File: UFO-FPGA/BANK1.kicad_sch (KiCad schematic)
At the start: 7 parts, among them U1 ICE40HX8K-BG121

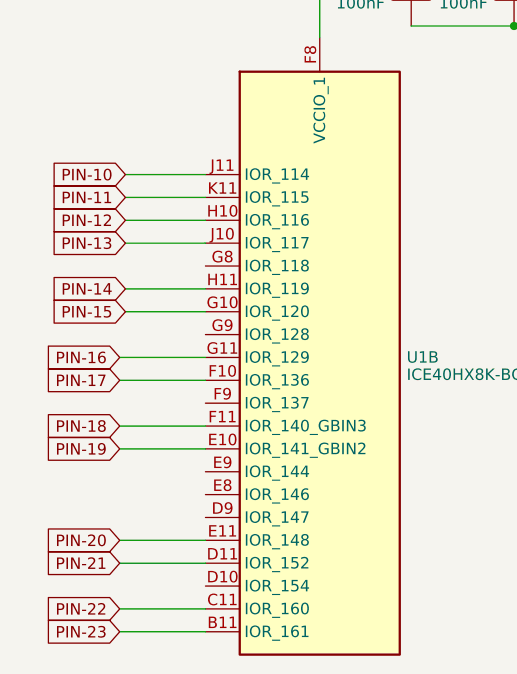
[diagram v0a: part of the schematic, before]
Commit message: Opamp gemaakt van de ADC
Enkel nog begrijpen wat VDC is. Aan docent vragen?
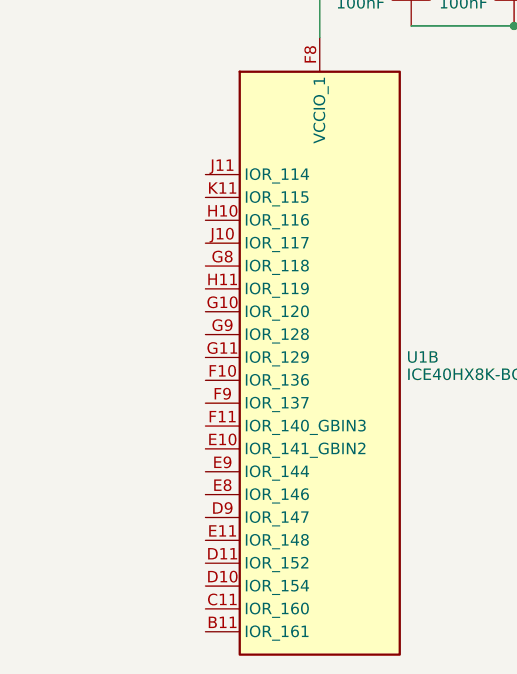
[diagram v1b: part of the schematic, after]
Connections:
- net PIN-10: no longer names the net of U1.J11 (IOR_114)
- net PIN-11: no longer names the net of U1.K11 (IOR_115)
- net PIN-12: no longer names the net of U1.H10 (IOR_116)
- net PIN-13: no longer names the net of U1.J10 (IOR_117)
- net PIN-14: no longer names the net of U1.H11 (IOR_119)
- net PIN-15: no longer names the net of U1.G10 (IOR_120)
- net PIN-16: no longer names the net of U1.G11 (IOR_129)
- net PIN-17: no longer names the net of U1.F10 (IOR_136)
- net PIN-18: no longer names the net of U1.F11 (IOR_140_GBIN3)
- net PIN-19: no longer names the net of U1.E10 (IOR_141_GBIN2)
- net PIN-20: no longer names the net of U1.E11 (IOR_148)
- net PIN-21: no longer names the net of U1.D11 (IOR_152)
- net PIN-22: no longer names the net of U1.C11 (IOR_160)
- net PIN-23: no longer names the net of U1.B11 (IOR_161)
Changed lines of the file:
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@@
   (junction (at 168.91 38.1) (diameter 0) (color 0 0 0 0)
   )
-  (wire (pts (xy 100.965 110.49) (xy 110.49 110.49))
-    (stroke (width 0) (type default))
-  )
   (wire (pts (xy 156.21 38.1) (xy 144.78 38.1))
-    (stroke (width 0) (type default))
-  )
-  (wire (pts (xy 100.965 90.17) (xy 110.49 90.17))
-    (stroke (width 0) (type default))
-  )
-  (wire (pts (xy 101.6 62.23) (xy 110.49 62.23))
-    (stroke (width 0) (type default))
-  )
-  (wire (pts (xy 101.6 64.77) (xy 110.49 64.77))
-    (stroke (width 0) (type default))
-  )
-  (wire (pts (xy 101.6 67.31) (xy 110.49 67.31))
-    (stroke (width 0) (type default))
-  )
-  (wire (pts (xy 101.6 74.93) (xy 110.49 74.93))
     (stroke (width 0) (type default))
   )
@@
     (stroke (width 0) (type default))
   )
-  (wire (pts (xy 100.965 113.03) (xy 110.49 113.03))
-    (stroke (width 0) (type default))
-  )
   (wire (pts (xy 156.21 45.72) (xy 144.78 45.72))
-    (stroke (width 0) (type default))
-  )
-  (wire (pts (xy 100.965 92.71) (xy 110.49 92.71))
     (stroke (width 0) (type default))
   )
@@
     (stroke (width 0) (type default))
   )
-  (wire (pts (xy 101.6 77.47) (xy 110.49 77.47))
-    (stroke (width 0) (type default))
-  )
   (wire (pts (xy 168.91 38.1) (xy 179.07 38.1))
     (stroke (width 0) (type default))
@@
     (stroke (width 0) (type default))
   )
-  (wire (pts (xy 100.965 85.09) (xy 110.49 85.09))
-    (stroke (width 0) (type default))
-  )
   (wire (pts (xy 168.91 38.1) (xy 167.64 38.1))
-    (stroke (width 0) (type default))
-  )
-  (wire (pts (xy 100.965 105.41) (xy 110.49 105.41))
-    (stroke (width 0) (type default))
-  )
-  (wire (pts (xy 101.6 69.85) (xy 110.49 69.85))
-    (stroke (width 0) (type default))
-  )
-  (wire (pts (xy 100.965 82.55) (xy 110.49 82.55))
     (stroke (width 0) (type default))
   )
@@
     (stroke (width 0) (type default))
   )
-  (wire (pts (xy 100.965 102.87) (xy 110.49 102.87))
-    (stroke (width 0) (type default))
-  )
   (label "VCCIO_1" (at 123.19 38.1 0) (fields_autoplaced)
     (effects (font (size 1.27 1.27)) (justify left bottom))
   )
-  (global_label "PIN-20" (shape input) (at 100.965 102.87 180) (fields_autoplaced)
-    (effects (font (size 1.27 1.27)) (justify right))
-    (property "Intersheetrefs" "${INTERSHEET_REFS}" (at 90.8625 102.87 0)
-      (effects (font (size 1.27 1.27)) (justify right) hide)
-    )
-  )
-  (global_label "PIN-15" (shape input) (at 101.6 77.47 180) (fields_autoplaced)
-    (effects (font (size 1.27 1.27)) (justify right))
-    (property "Intersheetrefs" "${INTERSHEET_REFS}" (at 91.4975 77.47 0)
-      (effects (font (size 1.27 1.27)) (justify right) hide)
-    )
-  )
-  (global_label "PIN-10" (shape input) (at 101.6 62.23 180) (fields_autoplaced)
-    (effects (font (size 1.27 1.27)) (justify right))
-    (property "Intersheetrefs" "${INTERSHEET_REFS}" (at 91.4975 62.23 0)
-      (effects (font (size 1.27 1.27)) (justify right) hide)
-    )
-  )
-  (global_label "PIN-22" (shape input) (at 100.965 110.49 180) (fields_autoplaced)
-    (effects (font (size 1.27 1.27)) (justify right))
-    (property "Intersheetrefs" "${INTERSHEET_REFS}" (at 90.8625 110.49 0)
-      (effects (font (size 1.27 1.27)) (justify right) hide)
-    )
-  )
-  (global_label "PIN-11" (shape input) (at 101.6 64.77 180) (fields_autoplaced)
-    (effects (font (size 1.27 1.27)) (justify right))
-    (property "Intersheetrefs" "${INTERSHEET_REFS}" (at 91.4975 64.77 0)
-      (effects (font (size 1.27 1.27)) (justify right) hide)
-    )
-  )
-  (global_label "PIN-13" (shape input) (at 101.6 69.85 180) (fields_autoplaced)
-    (effects (font (size 1.27 1.27)) (justify right))
-    (property "Intersheetrefs" "${INTERSHEET_REFS}" (at 91.4975 69.85 0)
-      (effects (font (size 1.27 1.27)) (justify right) hide)
-    )
-  )
-  (global_label "PIN-18" (shape input) (at 100.965 90.17 180) (fields_autoplaced)
-    (effects (font (size 1.27 1.27)) (justify right))
-    (property "Intersheetrefs" "${INTERSHEET_REFS}" (at 90.8625 90.17 0)
-      (effects (font (size 1.27 1.27)) (justify right) hide)
-    )
-  )
-  (global_label "PIN-19" (shape input) (at 100.965 92.71 180) (fields_autoplaced)
-    (effects (font (size 1.27 1.27)) (justify right))
-    (property "Intersheetrefs" "${INTERSHEET_REFS}" (at 90.8625 92.71 0)
-      (effects (font (size 1.27 1.27)) (justify right) hide)
-    )
-  )
-  (global_label "PIN-14" (shape input) (at 101.6 74.93 180) (fields_autoplaced)
-    (effects (font (size 1.27 1.27)) (justify right))
-    (property "Intersheetrefs" "${INTERSHEET_REFS}" (at 91.4975 74.93 0)
-      (effects (font (size 1.27 1.27)) (justify right) hide)
-    )
-  )
-  (global_label "PIN-12" (shape input) (at 101.6 67.31 180) (fields_autoplaced)
-    (effects (font (size 1.27 1.27)) (justify right))
-    (property "Intersheetrefs" "${INTERSHEET_REFS}" (at 91.4975 67.31 0)
-      (effects (font (size 1.27 1.27)) (justify right) hide)
-    )
-  )
-  (global_label "PIN-16" (shape input) (at 100.965 82.55 180) (fields_autoplaced)
-    (effects (font (size 1.27 1.27)) (justify right))
-    (property "Intersheetrefs" "${INTERSHEET_REFS}" (at 90.8625 82.55 0)
-      (effects (font (size 1.27 1.27)) (justify right) hide)
-    )
-  )
-  (global_label "PIN-17" (shape input) (at 100.965 85.09 180) (fields_autoplaced)
-    (effects (font (size 1.27 1.27)) (justify right))
-    (property "Intersheetrefs" "${INTERSHEET_REFS}" (at 90.8625 85.09 0)
-      (effects (font (size 1.27 1.27)) (justify right) hide)
-    )
-  )
-  (global_label "PIN-23" (shape input) (at 100.965 113.03 180) (fields_autoplaced)
-    (effects (font (size 1.27 1.27)) (justify right))
-    (property "Intersheetrefs" "${INTERSHEET_REFS}" (at 90.8625 113.03 0)
-      (effects (font (size 1.27 1.27)) (justify right) hide)
-    )
-  )
-  (global_label "PIN-21" (shape input) (at 100.965 105.41 180) (fields_autoplaced)
-    (effects (font (size 1.27 1.27)) (justify right))
-    (property "Intersheetrefs" "${INTERSHEET_REFS}" (at 90.8625 105.41 0)
-      (effects (font (size 1.27 1.27)) (justify right) hide)
-    )
-  )
   (symbol (lib_id "FPGA_Lattice:ICE40HX8K-BG121") (at 123.19 82.55 0) (unit 2)

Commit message: IO and power
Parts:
- removed C17 (x3): 100nF, symbol Device:C
- added C17 (x3): 100nF, symbol Device:C
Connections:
- net GND: now also C17.2, C17.2, C17.2
- net VCCIO_1: now also C17.1, C17.1, C17.1
- net PIN-23: now reaches U1.B11 (IOR_161)
- net PIN-22: now reaches U1.C11 (IOR_160)
- net PIN-21: now reaches U1.D11 (IOR_152)
- net PIN-19: now reaches U1.E10 (IOR_141_GBIN2)
- net PIN-20: now reaches U1.E11 (IOR_148)
- net PIN-17: now reaches U1.F10 (IOR_136)
- net PIN-18: now reaches U1.F11 (IOR_140_GBIN3)
- net PIN-15: now reaches U1.G10 (IOR_120)
- net PIN-16: now reaches U1.G11 (IOR_129)
- net PIN-12: now reaches U1.H10 (IOR_116)
- net PIN-14: now reaches U1.H11 (IOR_119)
- net PIN-13: now reaches U1.J10 (IOR_117)
- net PIN-10: now reaches U1.J11 (IOR_114)
- net PIN-11: now reaches U1.K11 (IOR_115)

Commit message: Revision
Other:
- company: (none) -> Universal-Field-Objects
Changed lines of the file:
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@@
   (paper "A4")
   (title_block
-    (date "2023-04-22")
-    (rev "V0.1")
+    (date "2023-04-25")
+    (rev "V0.5")
+    (company "Universal-Field-Objects")
   )
   (junction (at 182.88 55.88) (diameter 0) (color 0 0 0 0)

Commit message: footprints and PCB
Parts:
- R25: footprint (none) -> Resistor_SMD:R_0805_2012Metric_Pad1.20x1.40mm_HandSolder
- TP8: footprint (none) -> TestPoint:TestPoint_Keystone_5000-5004_Miniature
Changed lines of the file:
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@@
       (effects (font (size 1.27 1.27)) (justify left))
     )
-    (property "Footprint" "" (at 189.23 48.26 0)
+    (property "Footprint" "TestPoint:TestPoint_Keystone_5000-5004_Miniature" (at 189.23 48.26 0)
       (effects (font (size 1.27 1.27)) hide)
     )
@@
       (effects (font (size 1.27 1.27)))
     )
-    (property "Footprint" "" (at 198.12 46.482 90)
+    (property "Footprint" "Resistor_SMD:R_0805_2012Metric_Pad1.20x1.40mm_HandSolder" (at 198.12 46.482 90)
       (effects (font (size 1.27 1.27)) hide)
     )

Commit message: footprint
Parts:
- C17, C18: footprint (none) -> Capacitor_SMD:C_0805_2012Metric_Pad1.18x1.45mm_HandSolder
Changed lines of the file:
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@@
       (effects (font (size 1.27 1.27)) (justify left))
     )
-    (property "Footprint" "" (at 147.6248 55.88 0)
+    (property "Footprint" "Capacitor_SMD:C_0805_2012Metric_Pad1.18x1.45mm_HandSolder" (at 147.6248 55.88 0)
       (effects (font (size 1.27 1.27)) hide)
     )
@@
       (effects (font (size 1.27 1.27)) (justify left))
     )
-    (property "Footprint" "" (at 181.9148 55.88 0)
+    (property "Footprint" "Capacitor_SMD:C_0805_2012Metric_Pad1.18x1.45mm_HandSolder" (at 181.9148 55.88 0)
       (effects (font (size 1.27 1.27)) hide)
     )
@@
       (effects (font (size 1.27 1.27)) (justify left))
     )
-    (property "Footprint" "" (at 170.4848 55.88 0)
+    (property "Footprint" "Capacitor_SMD:C_0805_2012Metric_Pad1.18x1.45mm_HandSolder" (at 170.4848 55.88 0)
       (effects (font (size 1.27 1.27)) hide)
     )
@@
       (effects (font (size 1.27 1.27)) (justify left))
     )
-    (property "Footprint" "" (at 159.0548 55.88 0)
+    (property "Footprint" "Capacitor_SMD:C_0805_2012Metric_Pad1.18x1.45mm_HandSolder" (at 159.0548 55.88 0)
       (effects (font (size 1.27 1.27)) hide)
     )

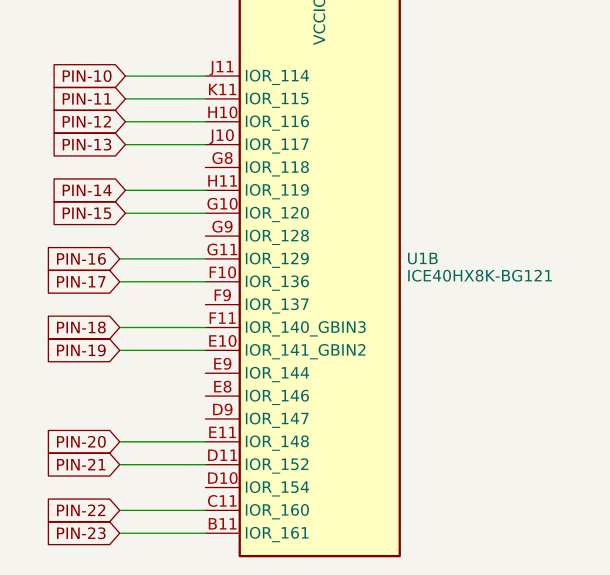
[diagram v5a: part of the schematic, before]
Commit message: PCB planes
Added:
added Power plane +1v2, +3v3 and +5v on layer 4
Ground plane on layer 2 and 5
Added signal layer 1,3 and 6
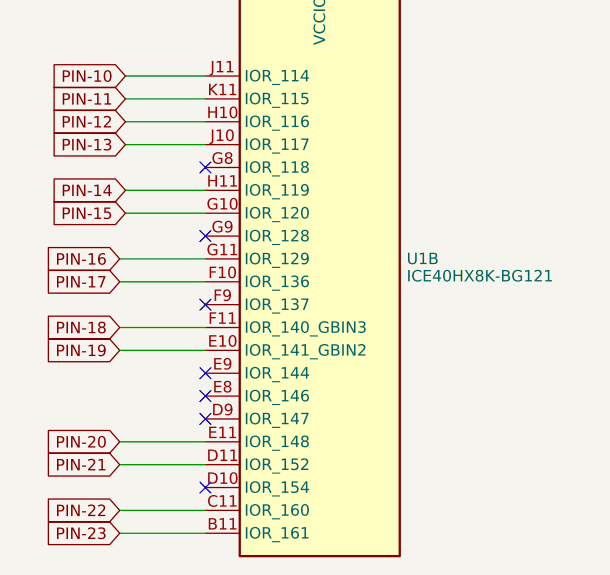
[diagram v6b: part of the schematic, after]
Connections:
- no-connect marks 0 -> 7
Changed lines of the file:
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@@
   (junction (at 171.45 48.26) (diameter 0) (color 0 0 0 0)
   )
+  (no_connect (at 125.73 118.11))
+  (no_connect (at 125.73 82.55))
+  (no_connect (at 125.73 105.41))
+  (no_connect (at 125.73 97.79))
+  (no_connect (at 125.73 90.17))
+  (no_connect (at 125.73 110.49))
+  (no_connect (at 125.73 107.95))
   (wire (pts (xy 116.84 80.01) (xy 125.73 80.01))
     (stroke (width 0) (type default))

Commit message: PCB
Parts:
- TP8: footprint TestPoint:TestPoint_Keystone_5000-5004_Miniature -> TestPoint:TestPoint_Pad_1.5x1.5mm
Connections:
- net PIN-10: no longer U1.J11 (IOR_114)
- net PIN-11: no longer U1.K11 (IOR_115)
- net PIN-12: no longer U1.H10 (IOR_116)
- net PIN-13: no longer U1.J10 (IOR_117)
- net PIN-14: no longer U1.H11 (IOR_119)
- net PIN-15: no longer U1.G10 (IOR_120)
- net PIN-16: no longer U1.G11 (IOR_129)
- net PIN-17: no longer U1.F10 (IOR_136)
- net PIN-18: no longer U1.F11 (IOR_140_GBIN3)
- net PIN-19: no longer U1.E10 (IOR_141_GBIN2)
- net PIN-20: no longer U1.E11 (IOR_148)
- net PIN-21: no longer U1.D11 (IOR_152)
- net PIN-22: no longer U1.C11 (IOR_160)
- net PIN-23: no longer U1.B11 (IOR_161)
- net +1V2 renamed +3V3

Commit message: PCB
many pcb changes
-started routing
-added vias
-power planes
-ground planes
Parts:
- removed C17 (x3): 100nF, Capacitor_SMD:C_0805_2012Metric_Pad1.18x1.45mm_HandSolder, symbol Device:C
- removed R25: 1, Resistor_SMD:R_0805_2012Metric_Pad1.20x1.40mm_HandSolder, symbol Device:R
- added C17: 200nF, Capacitor_SMD:C_0805_2012Metric_Pad1.18x1.45mm_HandSolder, symbol Device:C
- added R29: 0, Resistor_SMD:R_0805_2012Metric_Pad1.20x1.40mm_HandSolder, symbol Device:R
- C18: value 100nF -> 200nF
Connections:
- net +3V3: now also R29.2
- net GND: now also C17.2
- net VCCIO_1: now also C17.1, R29.1
